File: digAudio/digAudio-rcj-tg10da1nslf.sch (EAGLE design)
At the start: 12 parts, among them IC1 DIT4096-H

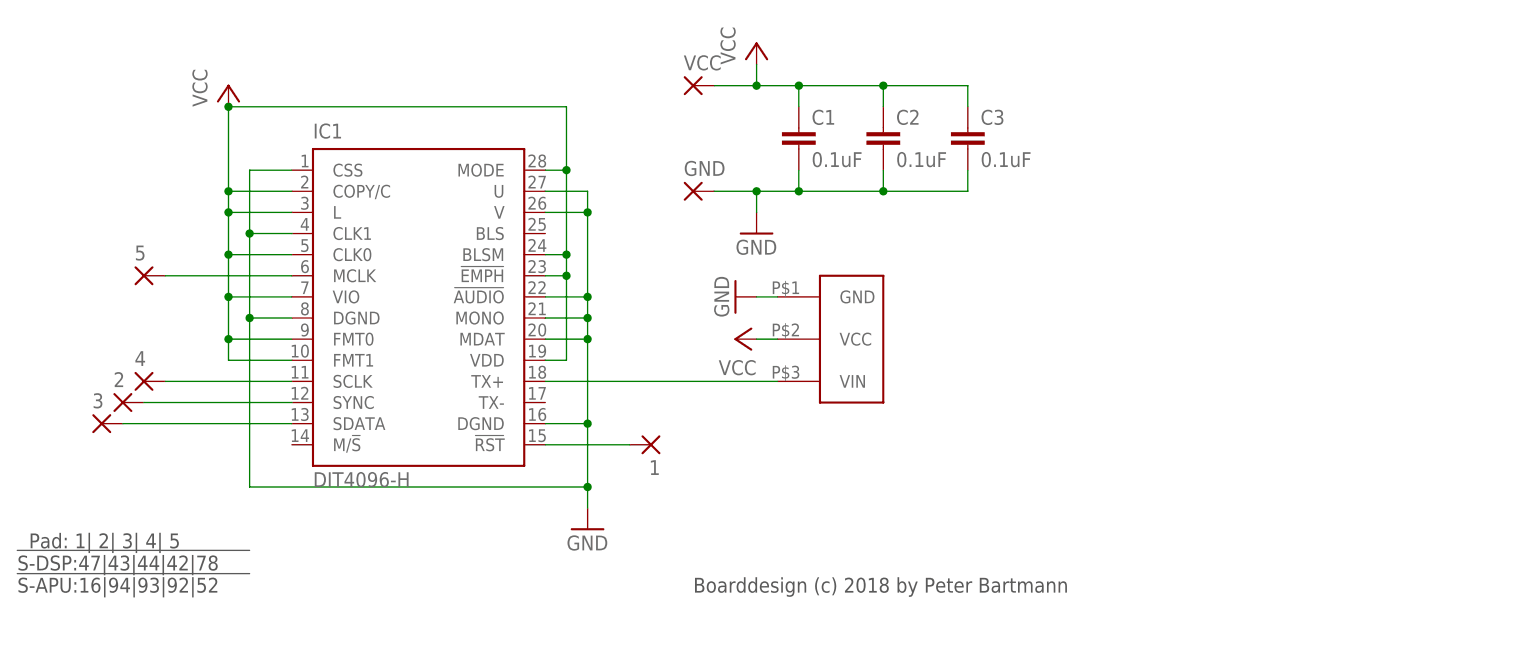
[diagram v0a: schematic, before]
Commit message: update digital audio mod incl a new no-cut design with coax
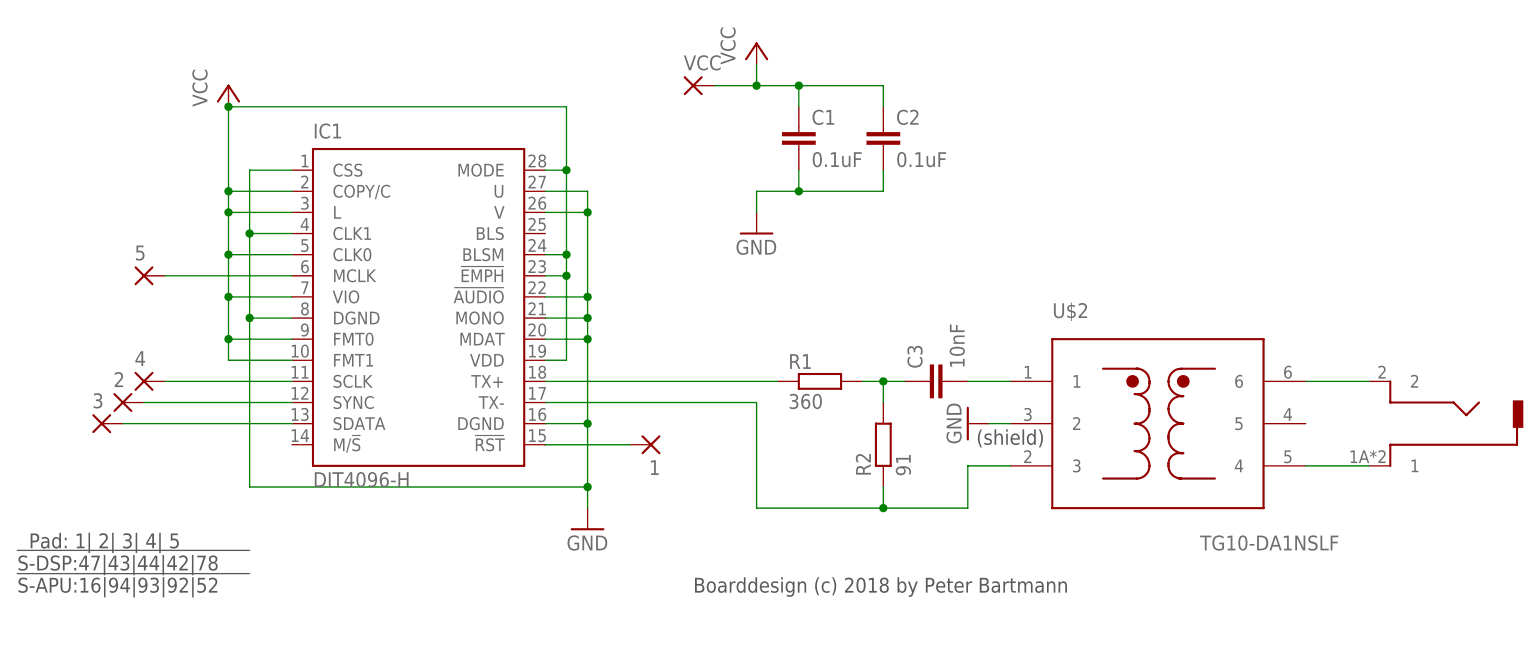
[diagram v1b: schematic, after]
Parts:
- removed GND: (no value), wirepad:SMD2
- added R1: 360, rcl:R-EU_R0603
- added R2: 91, rcl:R-EU_R0603
- added U$2: TG10-DA1NSLF, cs8406:TG10-DA1NSLF
- C3: value 0.1uF -> 10nF
- U$1: value PLT133/T10W -> RCJ-013-SMT-TR; device cs8406:PLT133/T10W -> digAudio_SNES:RCJ_01X_SMT-MODIFIED
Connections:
- new net N$10: U$1.1, U$2.4
- new net N$11: C3.2, U$2.1
- new net N$7: IC1.TX-, R2.1, U$2.3
- new net N$8: C3.1, R1.2, R2.2
- new net N$9: U$1.2, U$2.6
- net GND: now also U$2.2; no longer C3.2, GND.P, U$1.GND
- net N$1: now also R1.1; no longer U$1.VIN
- net VCC: no longer C3.1, U$1.VCC
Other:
- note added: "(shield)"
- moved on the sheet: C3
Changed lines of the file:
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@@
 </classes>
 <parts>
-<part name="VCC" library="wirepad" deviceset="SMD2" device=""/>
-<part name="GND" library="wirepad" deviceset="SMD2" device=""/>
+<part name="VCC" library="wirepad" library_urn="urn:adsk.eagle:library:412" deviceset="SMD2" device="" package3d_urn="urn:adsk.eagle:package:30839/1"/>
 <part name="IC1" library="texas" library_urn="urn:adsk.eagle:library:387" deviceset="DIT4192-H" device="" value="DIT4096-H"/>
 <part name="P+1" library="supply1" library_urn="urn:adsk.eagle:library:371" deviceset="VCC" device=""/>
 <part name="GND1" library="supply1" library_urn="urn:adsk.eagle:library:371" deviceset="GND" device=""/>
 <part name="GND2" library="supply1" library_urn="urn:adsk.eagle:library:371" deviceset="GND" device=""/>
-<part name="P+4" library="supply1" library_urn="urn:adsk.eagle:library:371" deviceset="VCC" device=""/>
-<part name="GND4" library="supply1" library_urn="urn:adsk.eagle:library:371" deviceset="GND" device=""/>
 <part name="C1" library="rcl" deviceset="C-EU" device="C0603" value="0.1uF"/>
 <part name="C2" library="rcl" deviceset="C-EU" device="C0603" value="0.1uF"/>
-<part name="C3" library="rcl" deviceset="C-EU" device="C0603" value="0.1uF"/>
+<part name="C3" library="rcl" deviceset="C-EU" device="C0603" value="10nF"/>
 <part name="P+5" library="supply1" library_urn="urn:adsk.eagle:library:371" deviceset="VCC" device=""/>
-<part name="5" library="wirepad" deviceset="SMD1" device="" value=""/>
-<part name="4" library="wirepad" deviceset="SMD1" device="" value=""/>
-<part name="2" library="wirepad" deviceset="SMD1" device="" value=""/>
-<part name="3" library="wirepad" deviceset="SMD1" device="" value=""/>
-<part name="1" library="wirepad" deviceset="SMD1" device="" value=""/>
-<part name="U$1" library="cs8406" deviceset="PLT133/T10W" device=""/>
+<part name="5" library="wirepad" library_urn="urn:adsk.eagle:library:412" deviceset="SMD1" device="" value=""/>
+<part name="4" library="wirepad" library_urn="urn:adsk.eagle:library:412" deviceset="SMD1" device="" value=""/>
+<part name="2" library="wirepad" library_urn="urn:adsk.eagle:library:412" deviceset="SMD1" device="" value=""/>
+<part name="3" library="wirepad" library_urn="urn:adsk.eagle:library:412" deviceset="SMD1" device="" value=""/>
+<part name="1" library="wirepad" library_urn="urn:adsk.eagle:library:412" deviceset="SMD1" device="" value=""/>
+<part name="U$1" library="digAudio_SNES" deviceset="RCJ_01X_SMT" device="-MODIFIED" value="RCJ-013-SMT-TR "/>
+<part name="R1" library="rcl" deviceset="R-EU_" device="R0603" value="360"/>
+<part name="R2" library="rcl" deviceset="R-EU_" device="R0603" value="91"/>
+<part name="U$2" library="cs8406" deviceset="TG10-DA1NSLF" device=""/>
+<part name="GND3" library="supply1" library_urn="urn:adsk.eagle:library:371" deviceset="GND" device=""/>
 </parts>
 <sheets>
@@
 <wire x1="-30.48" y1="17.526" x2="-2.54" y2="17.526" width="0.1524" layer="97"/>
 <text x="50.8" y="15.24" size="1.778" layer="97" font="vector">Boarddesign (c) 2018 by Peter Bartmann</text>
+<text x="84.836" y="33.02" size="1.778" layer="97">(shield)</text>
 </plain>
 <instances>
 <instance part="VCC" gate="1" x="50.8" y="76.2"/>
-<instance part="GND" gate="1" x="50.8" y="63.5"/>
 <instance part="IC1" gate="G$1" x="17.78" y="50.8"/>
 <instance part="P+1" gate="VCC" x="58.42" y="81.28"/>
 <instance part="GND1" gate="1" x="38.1" y="22.86"/>
 <instance part="GND2" gate="1" x="58.42" y="58.42"/>
-<instance part="P+4" gate="VCC" x="55.88" y="45.72" rot="R90"/>
-<instance part="GND4" gate="1" x="55.88" y="50.8" rot="R270"/>
 <instance part="C1" gate="G$1" x="63.5" y="71.12"/>
 <instance part="C2" gate="G$1" x="73.66" y="71.12"/>
-<instance part="C3" gate="G$1" x="83.82" y="71.12"/>
+<instance part="C3" gate="G$1" x="78.74" y="40.64" rot="R90"/>
 <instance part="P+5" gate="VCC" x="-5.08" y="76.2"/>
 <instance part="5" gate="G$1" x="-15.24" y="53.34"/>
@@
 <instance part="3" gate="G$1" x="-20.32" y="35.56"/>
 <instance part="1" gate="G$1" x="45.72" y="33.02" rot="R180"/>
-<instance part="U$1" gate="G$1" x="68.58" y="45.72"/>
+<instance part="U$1" gate="G$1" x="134.62" y="38.1" rot="R180"/>
+<instance part="R1" gate="G$1" x="66.04" y="40.64"/>
+<instance part="R2" gate="G$1" x="73.66" y="33.02" rot="R90"/>
+<instance part="U$2" gate="G$1" x="106.68" y="35.56"/>
+<instance part="GND3" gate="1" x="83.82" y="35.56" rot="R270"/>
 </instances>
 <busses>
@@
 <wire x1="60.96" y1="40.64" x2="33.02" y2="40.64" width="0.1524" layer="91"/>
 <pinref part="IC1" gate="G$1" pin="TX+"/>
-<pinref part="U$1" gate="G$1" pin="VIN"/>
+<pinref part="R1" gate="G$1" pin="1"/>
 </segment>
 </net>
 <net name="GND" class="0">
-<segment>
-<wire x1="58.42" y1="50.8" x2="60.96" y2="50.8" width="0.1524" layer="91"/>
-<pinref part="GND4" gate="1" pin="GND"/>
-<pinref part="U$1" gate="G$1" pin="GND"/>
-</segment>
 <segment>
 <pinref part="IC1" gate="G$1" pin="V"/>
@@
 </segment>
 <segment>
-<pinref part="GND" gate="1" pin="P"/>
 <pinref part="GND2" gate="1" pin="GND"/>
-<wire x1="53.34" y1="63.5" x2="58.42" y2="63.5" width="0.1524" layer="91"/>
 <wire x1="58.42" y1="63.5" x2="58.42" y2="60.96" width="0.1524" layer="91"/>
 <pinref part="C2" gate="G$1" pin="2"/>
@@
 <wire x1="63.5" y1="63.5" x2="73.66" y2="63.5" width="0.1524" layer="91"/>
 <wire x1="73.66" y1="63.5" x2="73.66" y2="66.04" width="0.1524" layer="91"/>
-<junction x="58.42" y="63.5"/>
 <pinref part="C1" gate="G$1" pin="2"/>
 <wire x1="63.5" y1="66.04" x2="63.5" y2="63.5" width="0.1524" layer="91"/>
 <junction x="63.5" y="63.5"/>
-<wire x1="73.66" y1="63.5" x2="83.82" y2="63.5" width="0.1524" layer="91"/>
-<junction x="73.66" y="63.5"/>
-<pinref part="C3" gate="G$1" pin="2"/>
-<wire x1="83.82" y1="63.5" x2="83.82" y2="66.04" width="0.1524" layer="91"/>
+</segment>
+<segment>
+<pinref part="U$2" gate="G$1" pin="2"/>
+<pinref part="GND3" gate="1" pin="GND"/>
+<wire x1="86.36" y1="35.56" x2="88.9" y2="35.56" width="0.1524" layer="91"/>
 </segment>
 </net>
@@
 <wire x1="63.5" y1="73.66" x2="63.5" y2="76.2" width="0.1524" layer="91"/>
 <junction x="63.5" y="76.2"/>
-<wire x1="73.66" y1="76.2" x2="83.82" y2="76.2" width="0.1524" layer="91"/>
-<wire x1="83.82" y1="76.2" x2="83.82" y2="73.66" width="0.1524" layer="91"/>
-<junction x="73.66" y="76.2"/>
-<pinref part="C3" gate="G$1" pin="1"/>
 </segment>
 <segment>
@@
 <junction x="-5.08" y="73.66"/>
 </segment>
-<segment>
-<wire x1="60.96" y1="45.72" x2="58.42" y2="45.72" width="0.1524" layer="91"/>
-<pinref part="P+4" gate="VCC" pin="VCC"/>
-<pinref part="U$1" gate="G$1" pin="VCC"/>
-</segment>
 </net>
 <net name="N$2" class="0">
@@
 <wire x1="2.54" y1="35.56" x2="-17.78" y2="35.56" width="0.1524" layer="91"/>
 <pinref part="3" gate="G$1" pin="P"/>
+</segment>
+</net>
+<net name="N$7" class="0">
+<segment>
+<pinref part="IC1" gate="G$1" pin="TX-"/>
+<wire x1="33.02" y1="38.1" x2="58.42" y2="38.1" width="0.1524" layer="91"/>
+<wire x1="58.42" y1="38.1" x2="58.42" y2="25.4" width="0.1524" layer="91"/>
+<pinref part="R2" gate="G$1" pin="1"/>
+<wire x1="58.42" y1="25.4" x2="73.66" y2="25.4" width="0.1524" layer="91"/>
+<wire x1="73.66" y1="25.4" x2="73.66" y2="27.94" width="0.1524" layer="91"/>
+<wire x1="73.66" y1="25.4" x2="83.82" y2="25.4" width="0.1524" layer="91"/>
+<junction x="73.66" y="25.4"/>
+<wire x1="83.82" y1="25.4" x2="83.82" y2="30.48" width="0.1524" layer="91"/>
+<pinref part="U$2" gate="G$1" pin="3"/>
+<wire x1="88.9" y1="30.48" x2="83.82" y2="30.48" width="0.1524" layer="91"/>
+</segment>
+</net>
+<net name="N$8" class="0">
+<segment>
+<pinref part="R1" gate="G$1" pin="2"/>
+<pinref part="C3" gate="G$1" pin="1"/>
+<wire x1="71.12" y1="40.64" x2="73.66" y2="40.64" width="0.1524" layer="91"/>
+<pinref part="R2" gate="G$1" pin="2"/>
+<wire x1="73.66" y1="40.64" x2="76.2" y2="40.64" width="0.1524" layer="91"/>
+<wire x1="73.66" y1="38.1" x2="73.66" y2="40.64" width="0.1524" layer="91"/>
+<junction x="73.66" y="40.64"/>
+</segment>
+</net>
+<net name="N$9" class="0">
+<segment>
+<pinref part="U$1" gate="G$1" pin="2"/>
+<pinref part="U$2" gate="G$1" pin="6"/>
+<wire x1="132.08" y1="40.64" x2="124.46" y2="40.64" width="0.1524" layer="91"/>
+</segment>
+</net>
+<net name="N$11" class="0">
+<segment>
+<pinref part="C3" gate="G$1" pin="2"/>
+<wire x1="88.9" y1="40.64" x2="83.82" y2="40.64" width="0.1524" layer="91"/>
+<pinref part="U$2" gate="G$1" pin="1"/>
+</segment>
+</net>
+<net name="N$10" class="0">
+<segment>
+<pinref part="U$2" gate="G$1" pin="4"/>
+<pinref part="U$1" gate="G$1" pin="1"/>
+<wire x1="132.08" y1="30.48" x2="124.46" y2="30.48" width="0.1524" layer="91"/>
 </segment>
 </net>
@@
 will not be understood (or retained) with this version.
 </note>
+<note version="8.3" severity="warning">
+Since Version 8.3, EAGLE supports the association of 3D packages
+with devices in libraries, schematics, and board files. Those 3D
+packages will not be understood (or retained) with this version.
+</note>
 </compatibility>

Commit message: PCB Update
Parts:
- added GND: (no value), wirepad:1,6/0,9
- added J1: (no value), jumper:SJ2W
- C3: value 10nF -> 10nF/0.1uF
- R1: value 360 -> 347.5/57
- R2: value 91 -> 90.9/open
- VCC: device wirepad:SMD2 -> wirepad:1,6/0,9
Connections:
- new net N$12: J1.2, R2.1, U$2.3
- net GND: now also GND.P, J1.1
- net N$7: now also J1.3; no longer R2.1, U$2.3
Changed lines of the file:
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@@
 <?xml version="1.0" encoding="utf-8"?>
 <!DOCTYPE eagle SYSTEM "eagle.dtd">
-<eagle version="8.6.0">
+<eagle version="8.5.2">
 <drawing>
 <settings>
@@
 </classes>
 <parts>
-<part name="VCC" library="wirepad" library_urn="urn:adsk.eagle:library:412" deviceset="SMD2" device="" package3d_urn="urn:adsk.eagle:package:30839/1"/>
 <part name="IC1" library="texas" library_urn="urn:adsk.eagle:library:387" deviceset="DIT4192-H" device="" value="DIT4096-H"/>
 <part name="P+1" library="supply1" library_urn="urn:adsk.eagle:library:371" deviceset="VCC" device=""/>
@@
 <part name="C1" library="rcl" deviceset="C-EU" device="C0603" value="0.1uF"/>
 <part name="C2" library="rcl" deviceset="C-EU" device="C0603" value="0.1uF"/>
-<part name="C3" library="rcl" deviceset="C-EU" device="C0603" value="10nF"/>
+<part name="C3" library="rcl" deviceset="C-EU" device="C0603" value="10nF/0.1uF"/>
 <part name="P+5" library="supply1" library_urn="urn:adsk.eagle:library:371" deviceset="VCC" device=""/>
 <part name="5" library="wirepad" library_urn="urn:adsk.eagle:library:412" deviceset="SMD1" device="" value=""/>
@@
 <part name="1" library="wirepad" library_urn="urn:adsk.eagle:library:412" deviceset="SMD1" device="" value=""/>
 <part name="U$1" library="digAudio_SNES" deviceset="RCJ_01X_SMT" device="-MODIFIED" value="RCJ-013-SMT-TR "/>
-<part name="R1" library="rcl" deviceset="R-EU_" device="R0603" value="360"/>
-<part name="R2" library="rcl" deviceset="R-EU_" device="R0603" value="91"/>
+<part name="R1" library="rcl" deviceset="R-EU_" device="R0603" value="347.5/57"/>
+<part name="R2" library="rcl" deviceset="R-EU_" device="R0603" value="90.9/open"/>
 <part name="U$2" library="cs8406" deviceset="TG10-DA1NSLF" device=""/>
 <part name="GND3" library="supply1" library_urn="urn:adsk.eagle:library:371" deviceset="GND" device=""/>
+<part name="VCC" library="wirepad" library_urn="urn:adsk.eagle:library:412" deviceset="1,6/0,9" device="" package3d_urn="urn:adsk.eagle:package:30840/1"/>
+<part name="GND" library="wirepad" library_urn="urn:adsk.eagle:library:412" deviceset="1,6/0,9" device="" package3d_urn="urn:adsk.eagle:package:30840/1"/>
+<part name="J1" library="jumper" library_urn="urn:adsk.eagle:library:252" deviceset="SJ2W" device="" package3d_urn="urn:adsk.eagle:package:15474/1"/>
+<part name="GND4" library="supply1" library_urn="urn:adsk.eagle:library:371" deviceset="GND" device=""/>
 </parts>
 <sheets>
@@
 <wire x1="-30.48" y1="20.32" x2="-2.54" y2="20.32" width="0.1524" layer="97"/>
 <wire x1="-30.48" y1="17.526" x2="-2.54" y2="17.526" width="0.1524" layer="97"/>
-<text x="50.8" y="15.24" size="1.778" layer="97" font="vector">Boarddesign (c) 2018 by Peter Bartmann</text>
+<text x="43.18" y="10.16" size="1.778" layer="97" font="vector">Boarddesign (c) 2018 by Peter Bartmann</text>
 <text x="84.836" y="33.02" size="1.778" layer="97">(shield)</text>
 </plain>
 <instances>
-<instance part="VCC" gate="1" x="50.8" y="76.2"/>
 <instance part="IC1" gate="G$1" x="17.78" y="50.8"/>
 <instance part="P+1" gate="VCC" x="58.42" y="81.28"/>
@@
 <instance part="U$2" gate="G$1" x="106.68" y="35.56"/>
 <instance part="GND3" gate="1" x="83.82" y="35.56" rot="R270"/>
+<instance part="VCC" gate="1" x="50.8" y="76.2"/>
+<instance part="GND" gate="1" x="50.8" y="63.5"/>
+<instance part="J1" gate="G$1" x="68.58" y="25.4" rot="R180"/>
+<instance part="GND4" gate="1" x="68.58" y="17.78"/>
 </instances>
 <busses>
@@
 <wire x1="63.5" y1="66.04" x2="63.5" y2="63.5" width="0.1524" layer="91"/>
 <junction x="63.5" y="63.5"/>
+<pinref part="GND" gate="1" pin="P"/>
+<wire x1="58.42" y1="63.5" x2="53.34" y2="63.5" width="0.1524" layer="91"/>
+<junction x="58.42" y="63.5"/>
 </segment>
 <segment>
@@
 <wire x1="86.36" y1="35.56" x2="88.9" y2="35.56" width="0.1524" layer="91"/>
 </segment>
+<segment>
+<pinref part="J1" gate="G$1" pin="1"/>
+<pinref part="GND4" gate="1" pin="GND"/>
+</segment>
 </net>
 <net name="VCC" class="0">
@@
 <pinref part="P+1" gate="VCC" pin="VCC"/>
 <wire x1="58.42" y1="78.74" x2="58.42" y2="76.2" width="0.1524" layer="91"/>
-<pinref part="VCC" gate="1" pin="P"/>
 <wire x1="53.34" y1="76.2" x2="58.42" y2="76.2" width="0.1524" layer="91"/>
 <pinref part="C2" gate="G$1" pin="1"/>
@@
 <wire x1="63.5" y1="73.66" x2="63.5" y2="76.2" width="0.1524" layer="91"/>
 <junction x="63.5" y="76.2"/>
+<pinref part="VCC" gate="1" pin="P"/>
 </segment>
 <segment>
@@
 <segment>
 <pinref part="IC1" gate="G$1" pin="TX-"/>
-<wire x1="33.02" y1="38.1" x2="58.42" y2="38.1" width="0.1524" layer="91"/>
-<wire x1="58.42" y1="38.1" x2="58.42" y2="25.4" width="0.1524" layer="91"/>
-<pinref part="R2" gate="G$1" pin="1"/>
-<wire x1="58.42" y1="25.4" x2="73.66" y2="25.4" width="0.1524" layer="91"/>
-<wire x1="73.66" y1="25.4" x2="73.66" y2="27.94" width="0.1524" layer="91"/>
-<wire x1="73.66" y1="25.4" x2="83.82" y2="25.4" width="0.1524" layer="91"/>
-<junction x="73.66" y="25.4"/>
-<wire x1="83.82" y1="25.4" x2="83.82" y2="30.48" width="0.1524" layer="91"/>
-<pinref part="U$2" gate="G$1" pin="3"/>
-<wire x1="88.9" y1="30.48" x2="83.82" y2="30.48" width="0.1524" layer="91"/>
+<wire x1="33.02" y1="38.1" x2="60.96" y2="38.1" width="0.1524" layer="91"/>
+<wire x1="60.96" y1="38.1" x2="60.96" y2="35.56" width="0.1524" layer="91"/>
+<pinref part="J1" gate="G$1" pin="3"/>
+<wire x1="60.96" y1="35.56" x2="68.58" y2="35.56" width="0.1524" layer="91"/>
+<wire x1="68.58" y1="35.56" x2="68.58" y2="30.48" width="0.1524" layer="91"/>
 </segment>
 </net>
@@
 </segment>
 </net>
+<net name="N$12" class="0">
+<segment>
+<pinref part="U$2" gate="G$1" pin="3"/>
+<wire x1="88.9" y1="30.48" x2="83.82" y2="30.48" width="0.1524" layer="91"/>
+<wire x1="83.82" y1="25.4" x2="83.82" y2="30.48" width="0.1524" layer="91"/>
+<pinref part="R2" gate="G$1" pin="1"/>
+<wire x1="73.66" y1="25.4" x2="73.66" y2="27.94" width="0.1524" layer="91"/>
+<wire x1="73.66" y1="25.4" x2="83.82" y2="25.4" width="0.1524" layer="91"/>
+<junction x="73.66" y="25.4"/>
+<pinref part="J1" gate="G$1" pin="2"/>
+</segment>
+</net>
